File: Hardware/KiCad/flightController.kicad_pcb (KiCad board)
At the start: 4 copper layers, 60 x 60 mm, 161 parts, among them J1 USB_B_Mini, J10 JST SH1-2P, J11 MOLEX 5268-7P, J12 JST SH1-8P, J2 USB_B_Mini, J3 2.54mm header, J4 2.54mm header, J5 TF-01A, J6 1mm header, J7 JST SH1-4P, J8 JST SH1-4P, J9 JST SH1-4P, Q1 PMBT3904, Q2 PMBT3904, SW1 SW_SPDT, SW2 SW_Push, U1 MPU-6000, U10 CH330N, U11 SMF05CT1G, U12 SMF05CT1G, U13 SMF05CT1G, U2 HMC5883L, U3 FM24C64B, U4 BMP388, U5 STM32H743VIT6, U6 AMS1117-5V, U7 AMS1117-3.3, U8 SMF05CT1G, U9 SMF05CT1G

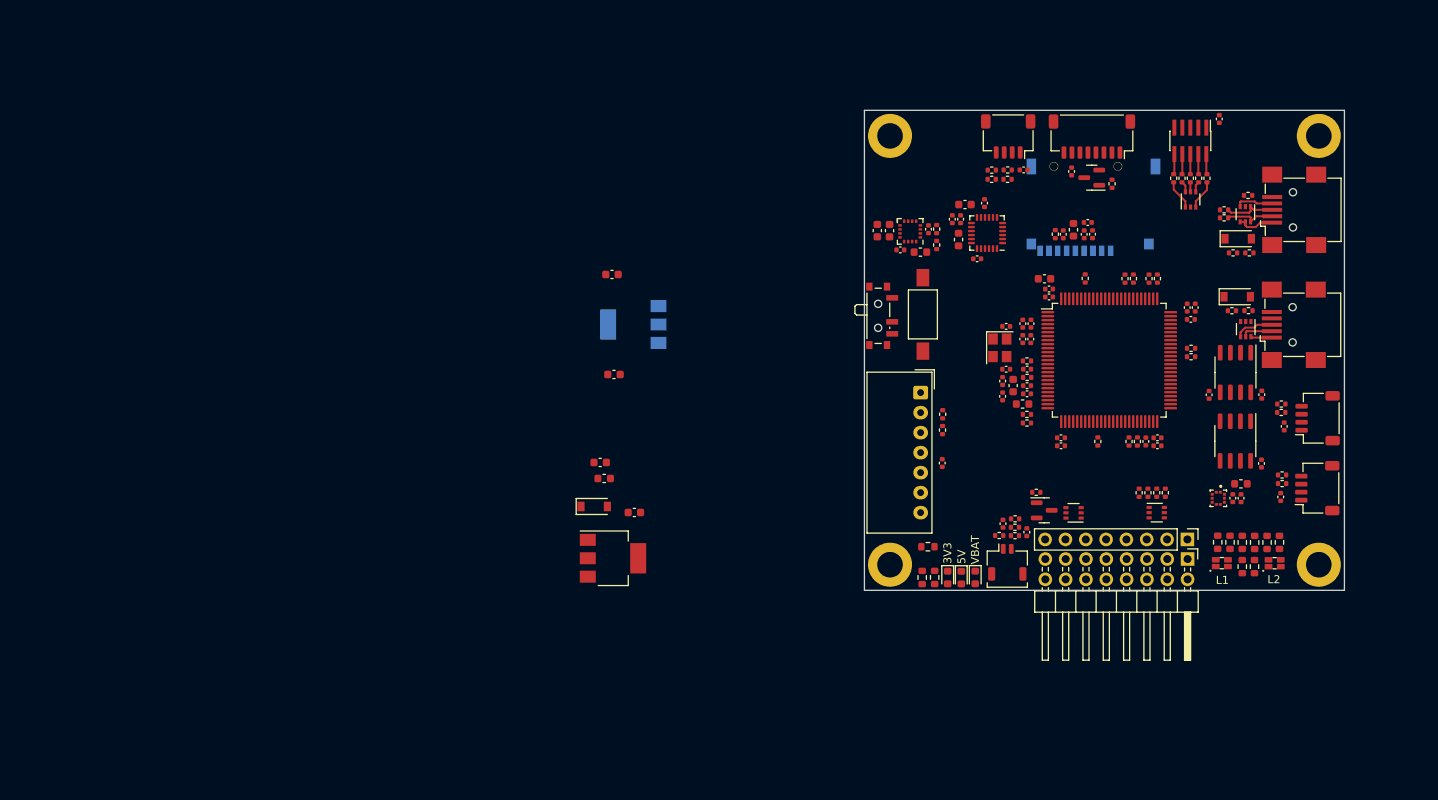
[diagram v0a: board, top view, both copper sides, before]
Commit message: Outline, component placement and some traces complete
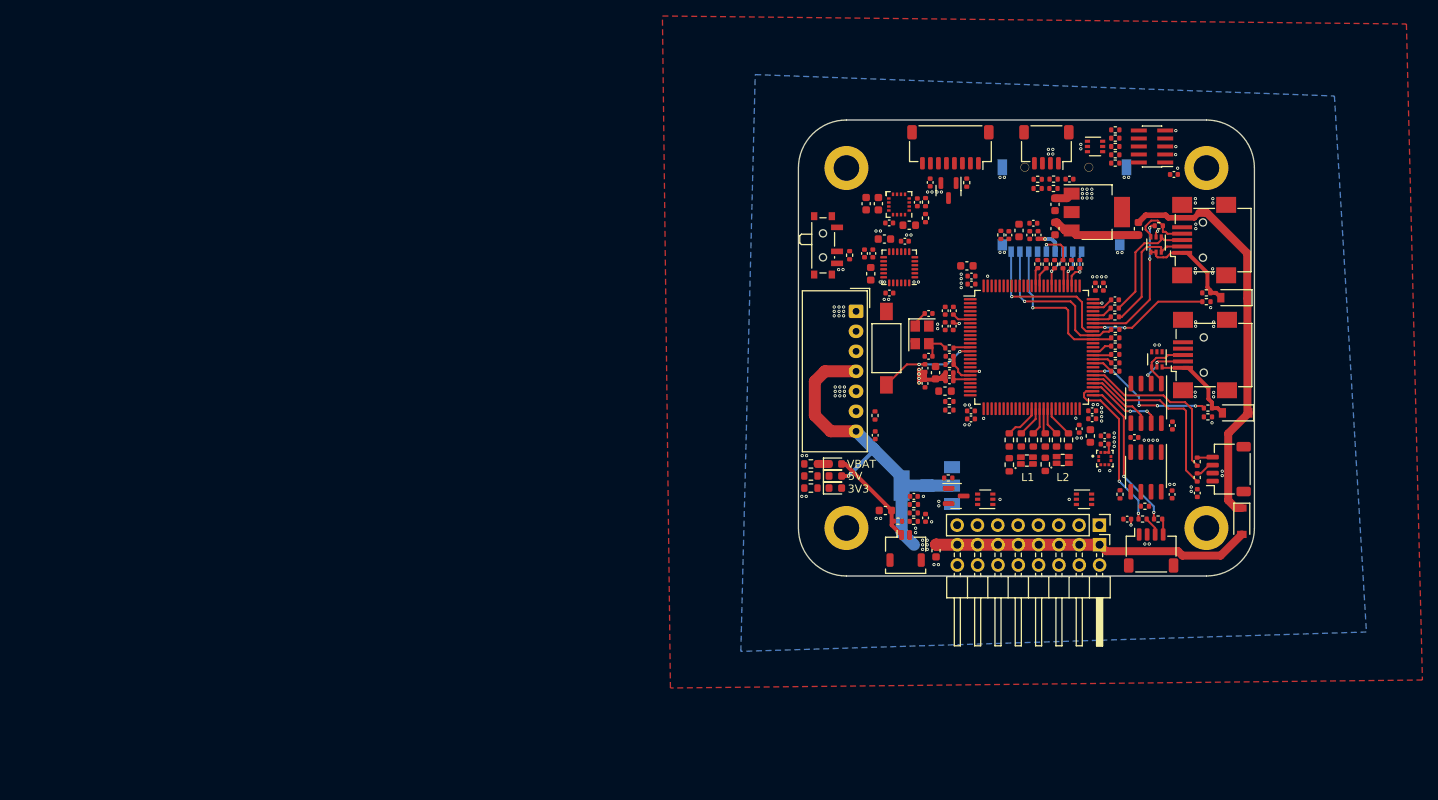
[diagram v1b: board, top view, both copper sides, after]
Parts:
- moved D6 81.0 mm to (222.4, 102.2), turned to -90 degrees
- moved U7 74.4 mm to (204.3, 63.5)
- moved FB4 73.7 mm to (209.5, 65.6), turned to -90 degrees
- moved C32 65.2 mm to (199.1, 62.5), turned to 90 degrees
- moved C31 63.9 mm to (199.1, 65.6), turned to -90 degrees
- moved H1 59.2 mm to (173.0, 103.0)
- moved H3 59.2 mm to (173.0, 58.0)
- moved C30 53.2 mm to (184.2, 105.8), turned to -90 degrees
- moved U6 41.8 mm to (183.1, 97.7)
- moved H2 39.8 mm to (218.0, 103.0)
- moved H4 39.8 mm to (218.0, 58.0)
- moved C29 38.0 mm to (177.9, 100.8), turned to 180 degrees
- moved R2 31.8 mm to (193.4, 95.1)
- moved R48 29.6 mm to (173.4, 68.9)
- moved D2 29.5 mm to (200.0, 94.5)
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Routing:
- net +5V: track 0.00 -> 86.2 mm, vias 0 -> 7
- net REG_IN: track 0.00 -> 50.3 mm
- net Net-(R19-Pad2): track 0.00 -> 22.7 mm
- net GND: track 0.00 -> 22.1 mm, vias 0 -> 151
- net Net-(R20-Pad2): track 0.00 -> 21.5 mm
- net SDIO_D1: track 0.00 -> 21.1 mm, vias 0 -> 1
- net Net-(R38-Pad1): track 0.00 -> 20.7 mm, vias 0 -> 2
- net SDIO_D0: track 0.00 -> 20.6 mm, vias 0 -> 1
- net SD_CARD_DETECT: track 0.00 -> 19.4 mm, vias 0 -> 1
- net Net-(R37-Pad1): track 0.00 -> 19.3 mm, vias 0 -> 2
- net USB_ID: track 0.00 -> 18.1 mm, vias 0 -> 2
- net USB_VBUS_DEBUG: track 0.00 -> 16.4 mm, vias 0 -> 4
- net USB_VBUS_PROG: track 0.00 -> 15.0 mm, vias 0 -> 2
- net VCC: track 0.00 -> 12.3 mm
- net Net-(C31-Pad1): track 0.00 -> 11.1 mm
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- added copper zone on B.Cu, net +3V3
- added copper zone on F.Cu, net +3V3
- added copper zone on In1.Cu, net GND
- added copper zone on In2.Cu, net GND
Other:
- board size 60 x 60 mm -> 57 x 57 mm

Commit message: Almost finished all routing
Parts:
- added TP13: TestPoint, TestPoint:TestPoint_Pad_D1.0mm, B.Cu at (181.1, 75.0)
- added TP14: TestPoint, TestPoint:TestPoint_Pad_D1.0mm, B.Cu at (183.2, 72.3)
- added TP15: TestPoint, TestPoint:TestPoint_Pad_D1.0mm, B.Cu at (183.2, 75.0)
- added TP16: TestPoint, TestPoint:TestPoint_Pad_D1.0mm, B.Cu at (176.5, 78.4)
- added TP17: TestPoint, TestPoint:TestPoint_Pad_D1.0mm, B.Cu at (176.5, 80.9)
- added TP18: TestPoint, TestPoint:TestPoint_Pad_D1.0mm, B.Cu at (218.8, 95.0)
- added TP19: TestPoint, TestPoint:TestPoint_Pad_D1.0mm, B.Cu at (218.8, 93.2)
- added TP20: TestPoint, TestPoint:TestPoint_Pad_D1.0mm, B.Cu at (212.2, 103.8)
- added TP21: TestPoint, TestPoint:TestPoint_Pad_D1.0mm, B.Cu at (214.1, 103.8)
- added TP22: TestPoint, TestPoint:TestPoint_Pad_D1.0mm, B.Cu at (146.1, 99.5)
- added TP23: TestPoint, TestPoint:TestPoint_Pad_D1.0mm, B.Cu at (174.2, 73.8)
- added TP24: TestPoint, TestPoint:TestPoint_Pad_D1.0mm, B.Cu at (139.1, 99.5)
- added TP25: TestPoint, TestPoint:TestPoint_Pad_D1.0mm, B.Cu at (141.3, 99.5)
- added TP26: TestPoint, TestPoint:TestPoint_Pad_D1.0mm, B.Cu at (143.8, 99.5)
- added TP28: TestPoint, TestPoint:TestPoint_Pad_D1.0mm, B.Cu at (174.4, 95.3)
- added TP29: TestPoint, TestPoint:TestPoint_Pad_D1.0mm, B.Cu at (174.4, 99.1)
- added TP3: TestPoint, TestPoint:TestPoint_Pad_D1.0mm, B.Cu at (205.4, 98.0)
- added TP30: TestPoint, TestPoint:TestPoint_Pad_D1.0mm, B.Cu at (171.2, 95.3)
- added TP31: TestPoint, TestPoint:TestPoint_Pad_D1.0mm, B.Cu at (171.2, 99.1)
- added TP4: TestPoint, TestPoint:TestPoint_Pad_D1.0mm, B.Cu at (209.8, 96.0)
- added TP5: TestPoint, TestPoint:TestPoint_Pad_D1.0mm, B.Cu at (185.0, 64.6)
- added TP6: TestPoint, TestPoint:TestPoint_Pad_D1.0mm, B.Cu at (187.2, 64.7)
- R1, R3, R4, R5, R7, R8: footprint Resistor_SMD:R_0603_1608Metric -> Resistor_SMD:R_0402_1005Metric
- moved SW2 10.1 mm to (179.9, 90.4), turned to -90 degrees
- moved R16 9.08 mm to (192.6, 90.8), turned to -90 degrees
- moved FB2 4.63 mm to (176.2, 64.8), turned to 0 degrees
- moved R6 4.20 mm to (201.8, 93.7)
- moved C6 2.51 mm to (180.4, 60.2), turned to 180 degrees
- moved R1 2.02 mm to (195.0, 90.8)
- moved Q1 1.82 mm to (186.5, 97.2)
- moved R3 1.68 mm to (196.1, 90.8)
- moved D1 1.51 mm to (196.1, 93.2)
- moved C1 1.50 mm to (176.2, 66.9)
- moved R35 1.50 mm to (197.4, 61.0), turned to 90 degrees
- moved D2 1.45 mm to (199.6, 93.1)
- moved R2 1.41 mm to (193.7, 93.7)
- moved R4 1.40 mm to (197.1, 90.8)
- moved R8 1.29 mm to (200.2, 90.8)
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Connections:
- U5 pad 31: unconnected-(U5-Pad31) -> BUZZ_ON
- U5 pad 63: BUZZ_ON -> unconnected-(U5-Pad63)
- U5 pad 91: LED_EXT -> unconnected-(U5-Pad91)
- U5 pad 98: unconnected-(U5-Pad98) -> LED_EXT
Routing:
- net GND: track 22.1 -> 116.7 mm, vias 151 -> 140
- net NRST: track 13.0 -> 54.8 mm, vias 2 -> 4
- net PWM3: track 0.00 -> 37.5 mm, vias 0 -> 4
- net USART2_TX: track 0.00 -> 37.1 mm, vias 0 -> 4
- net USART2_RX: track 0.00 -> 36.8 mm, vias 0 -> 4
- net +3V3: track 2.35 -> 38.1 mm, vias 0 -> 35
- net PWM2: track 0.00 -> 34.9 mm, vias 0 -> 4
- net PWM1: track 0.00 -> 34.3 mm, vias 0 -> 4
- net PWM0: track 0.00 -> 32.5 mm, vias 0 -> 4
- net SWO/TDO: track 0.00 -> 28.4 mm, vias 0 -> 2
- net SWDIO/TMS: track 0.00 -> 27.8 mm, vias 0 -> 6
- net BOOT0: track 0.00 -> 24.5 mm, vias 0 -> 2
- net TDI: track 0.00 -> 23.9 mm, vias 0 -> 2
- net PWM4: track 0.00 -> 21.7 mm, vias 0 -> 2
- net I2C2_SCL: track 0.00 -> 21.3 mm, vias 0 -> 4
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- added copper zone on B.Cu, net +5V
- added copper zone on B.Cu, net GND
- added copper zone on F.Cu, net GND
- added copper zone on B.Cu, net VCC
- added copper zone on F.Cu, net VCC
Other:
- outline, holes or cut-outs redrawn
- board text added: "0"
- board text added: "1"
- board text added: "2SCL"
- board text added: "2SDA"
- board text added: "3RX"
- board text added: "3TX"
- board text added: "4SCL"
- board text added: "4SDA"
- board text added: "5"
- board text added: "5RX"
- board text added: "5TX"
- board text added: "BAT"
- board text added: "BOOT0"
- board text added: "CL"
- board text added: "EXT LEDS"
- board text added: "GND"
- board text added: "I2C1"
- board text added: "MI"
- board text added: "MO"
- board text added: "MOTOR"
- board text added: "PWM"
- board text added: "RESET"
- board text added: "RPLIDAR"
- board text added: "RX"
- board text added: "S"
- board text added: "SWD"
- board text added: "TX"
- board text added: "UART3"
- board text added: "UART5"
- board text added: "USART2"
- board text added: "USB1"
- board text added: "USB2"

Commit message: Routing finished
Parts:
- J3: footprint Connector_PinHeader_2.54mm:PinHeader_1x08_P2.54mm_Vertical -> flightController:PinHeader_1x08_P2.54mm_Vertical_lessSilk
- J4: footprint Connector_PinHeader_2.54mm:PinHeader_2x08_P2.54mm_Horizontal -> flightController:PinHeader_2x08_P2.54mm_Horizontal_lessSilk
- U2: footprint Package_LGA:LGA-16_3x3mm_P0.5mm -> flightController:LGA-16_3x3mm_P0.5mm_Large_Pads
- moved R6 103.7 mm to (101.4, 119.5)
- moved D1 102.5 mm to (96.8, 118.8)
- moved C5 101.4 mm to (79.1, 94.4), turned to 90 degrees
- moved FB5 101.3 mm to (87.3, 111.6), turned to 90 degrees
- moved C34 100.8 mm to (85.6, 106.5)
- moved C33 100.8 mm to (85.7, 101.2)
- moved FB2 100.7 mm to (78.9, 90.7)
- moved U1 100.5 mm to (82.3, 95.6), turned to 90 degrees
- moved TP20 100.1 mm to (115.2, 128.8)
- moved TP18 100.1 mm to (122.0, 120.2)
- moved TP14 100.0 mm to (86.4, 97.4)
- moved C15 100.0 mm to (104.5, 115.8)
- moved C25 100.0 mm to (107.3, 97.9)
- moved C26 100.0 mm to (108.3, 97.9)
- moved C48 100.0 mm to (120.1, 123.7)
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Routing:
- net REG_IN: track 50.3 -> 0.00 mm
- net Net-(C31-Pad1): track 11.1 -> 0.23 mm, vias 0 -> 9
- net IMU_SCL: track 11.3 -> 17.7 mm
- net IMU_INT: track 16.7 -> 10.3 mm
- net Net-(D1-Pad1): track 0.00 -> 5.39 mm
- net Net-(D2-Pad4): track 0.00 -> 4.66 mm
- net IMU_MOSI: track 11.1 -> 15.3 mm
- net Net-(D2-Pad1): track 0.00 -> 4.16 mm
- net +3V3: track 38.1 -> 42.2 mm, vias 35 -> 115
- net Net-(D1-Pad2): track 0.00 -> 3.96 mm
- net BOOT0: track 24.5 -> 20.7 mm
- net Net-(D1-Pad3): track 0.00 -> 3.56 mm
- net Net-(R48-Pad2): track 1.58 -> 4.64 mm
- net GND: track 116.7 -> 113.8 mm
- net Net-(D1-Pad4): track 0.00 -> 2.72 mm
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- added copper zone on B.Cu, net Net-(C31-Pad1)
- added copper zone on F.Cu, net Net-(C31-Pad1)
- added copper zone on F.Cu, net REG_IN
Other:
- outline, holes or cut-outs redrawn
- board text added: "0V"
- board text added: "45 mm"
- board text added: "57 mm"
- board text added: "MAG"
- board text added: "RPLIDAR A1M8"
- board text added: "X"
- board text added: "Y"
- board text added: "Z"
- board text removed: "RPLIDAR"

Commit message: Added labels
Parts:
- moved D1 2.56 mm to (94.4, 119.5)
- moved R2 1.81 mm to (98.0, 119.7), turned to 90 degrees
- moved R6 1.81 mm to (99.6, 119.7), turned to 90 degrees
- moved D2 1.30 mm to (103.5, 119.5)
- moved C14 0.98 mm to (93.8, 115.8)
- moved R16 0.98 mm to (94.8, 115.7)
- moved C50 0.51 mm to (111.5, 126.4), turned to 90 degrees
- moved R42 0.47 mm to (113.0, 125.3)
- moved D6 0.31 mm to (125.4, 127.3)
- moved J2 0.24 mm to (120.6, 106.4)
- moved C10 0.20 mm to (116.7, 123.8)
- moved C12 0.20 mm to (108.3, 116.5)
- moved C13 0.20 mm to (85.9, 126.8)
- moved C15 0.20 mm to (104.3, 115.8)
- moved C16 0.20 mm to (109.6, 99.5)
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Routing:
- net +5V: track 97.2 -> 77.7 mm
- net Net-(J12-Pad1): track 14.7 -> 20.3 mm
- net Net-(D1-Pad2): track 3.96 -> 6.76 mm
- net Net-(D1-Pad3): track 3.56 -> 6.29 mm
- net Net-(D1-Pad1): track 5.39 -> 8.05 mm
- net IMU_SCL: track 17.7 -> 19.4 mm
- net Net-(D2-Pad4): track 4.66 -> 5.88 mm
- net GND: track 113.8 -> 112.6 mm
- net Net-(D1-Pad4): track 2.72 -> 3.48 mm
- net Net-(Q1-Pad1): track 9.87 -> 9.27 mm
- net +3V3: vias 115 -> 104
- added copper zone on F.Cu, net +5V
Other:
- outline, holes or cut-outs redrawn
- board text added: "RPLIDAR"

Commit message: Layout optimizations
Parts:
- moved FB6 2.33 mm to (98.1, 93.1), turned to 0 degrees
- moved C46 1.57 mm to (97.9, 91.4)
- moved R59 1.57 mm to (96.9, 91.4)
- moved C43 0.07 mm to (99.4, 89.9)
- moved C16 0.06 mm to (109.6, 99.5)
- moved R28 0.06 mm to (109.6, 101.6)
- moved R29 0.06 mm to (109.6, 100.5)

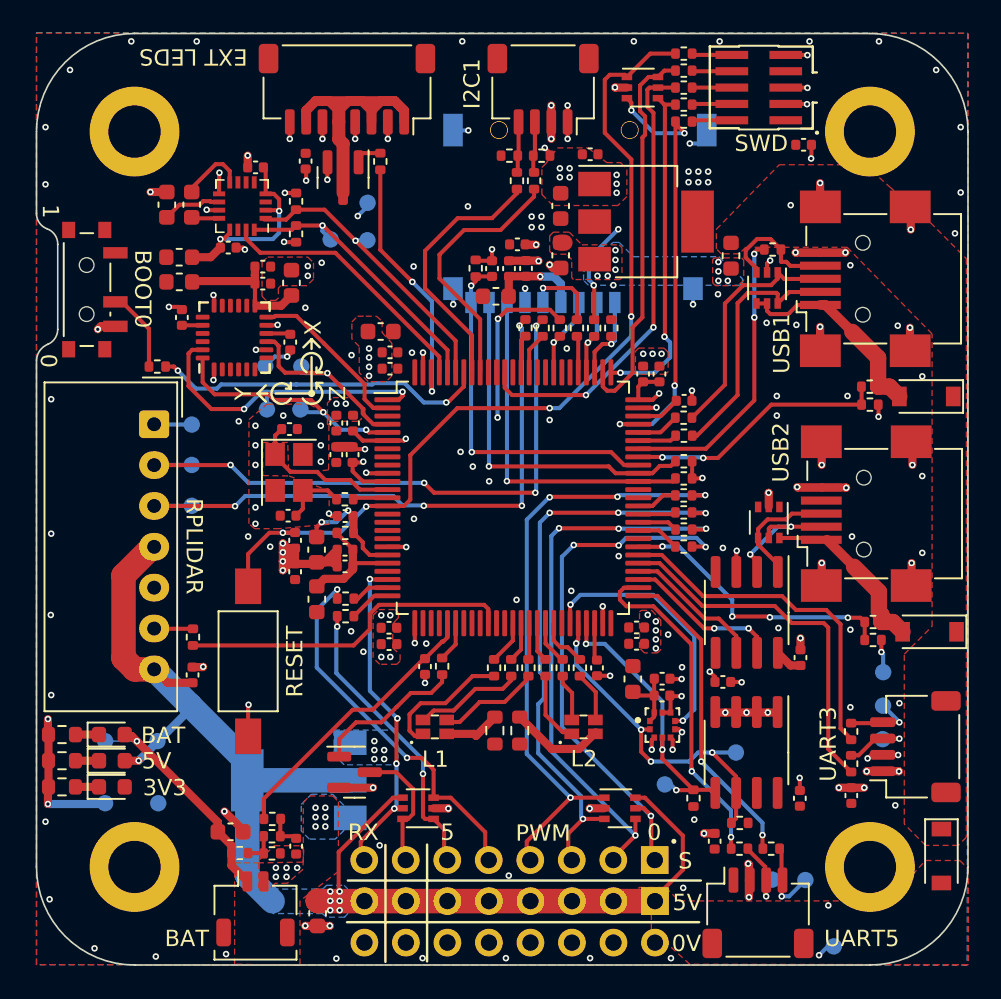
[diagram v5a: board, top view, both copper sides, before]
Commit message: Some small trace and layout optimisation
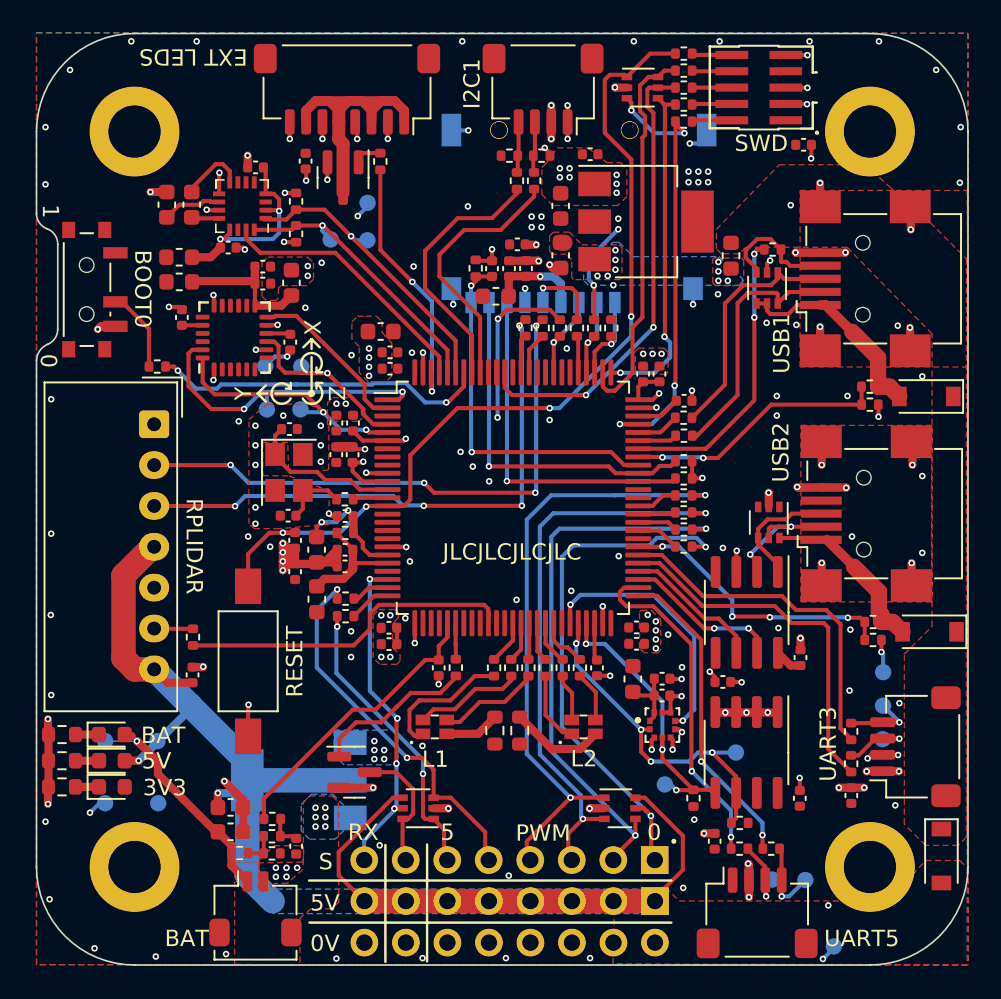
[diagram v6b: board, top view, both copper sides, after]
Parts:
- removed TP16, TP17, TP23: TestPoint, TestPoint:TestPoint_Pad_D1.0mm
- moved C30 8.39 mm to (81.9, 124.4), turned to 0 degrees
- moved C14 0.84 mm to (94.6, 115.8)
- moved R16 0.84 mm to (95.7, 115.8)
- moved J8 0.05 mm to (114.1, 130.8)
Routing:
- net GND: track 112.6 -> 108.7 mm, vias 140 -> 139
- net USART2_TX: track 37.1 -> 34.8 mm
- net USART2_RX: track 36.7 -> 34.4 mm
- net +3V3: track 42.2 -> 43.3 mm, vias 104 -> 103
- net +5V: track 77.7 -> 78.7 mm, vias 7 -> 2
- net Net-(J12-Pad1): track 20.3 -> 19.5 mm
- net Net-(Q1-Pad1): track 9.27 -> 9.87 mm
- net PWM2: track 35.0 -> 34.5 mm, vias 4 -> 2
- net PWM1: vias 4 -> 2
- net PWM0: vias 4 -> 2
- net PWM3: track 37.6 -> 37.5 mm, vias 4 -> 2
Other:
- board text added: "22/3/22"
- board text added: "JLCJLCJLCJLC"
- board text added: "MulticopterFCS"
- board text added: "V1.0"
- board text added: "by MatvBinn"
- board text removed: "USART2"
